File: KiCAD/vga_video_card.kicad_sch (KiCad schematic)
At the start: 4 parts, among them SW1 rst_btn, U5 74HC04, Y1 10MHz

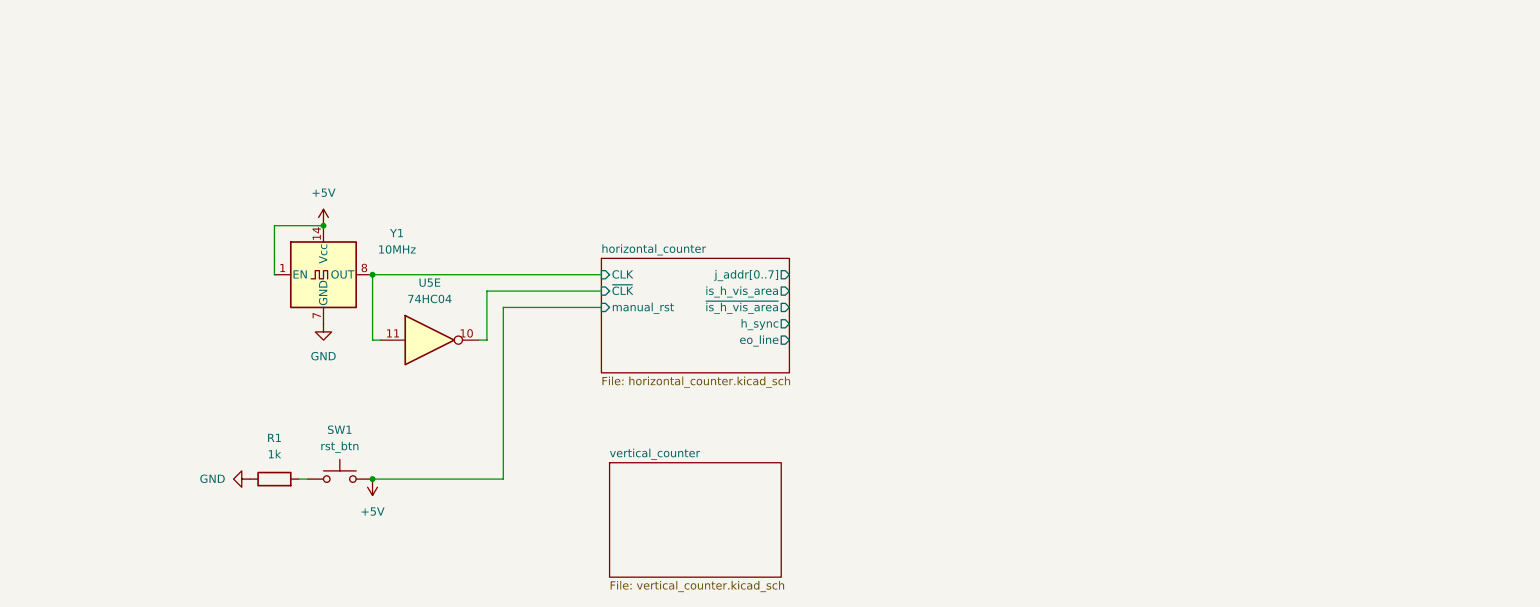
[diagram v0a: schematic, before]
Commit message: assigned footprints
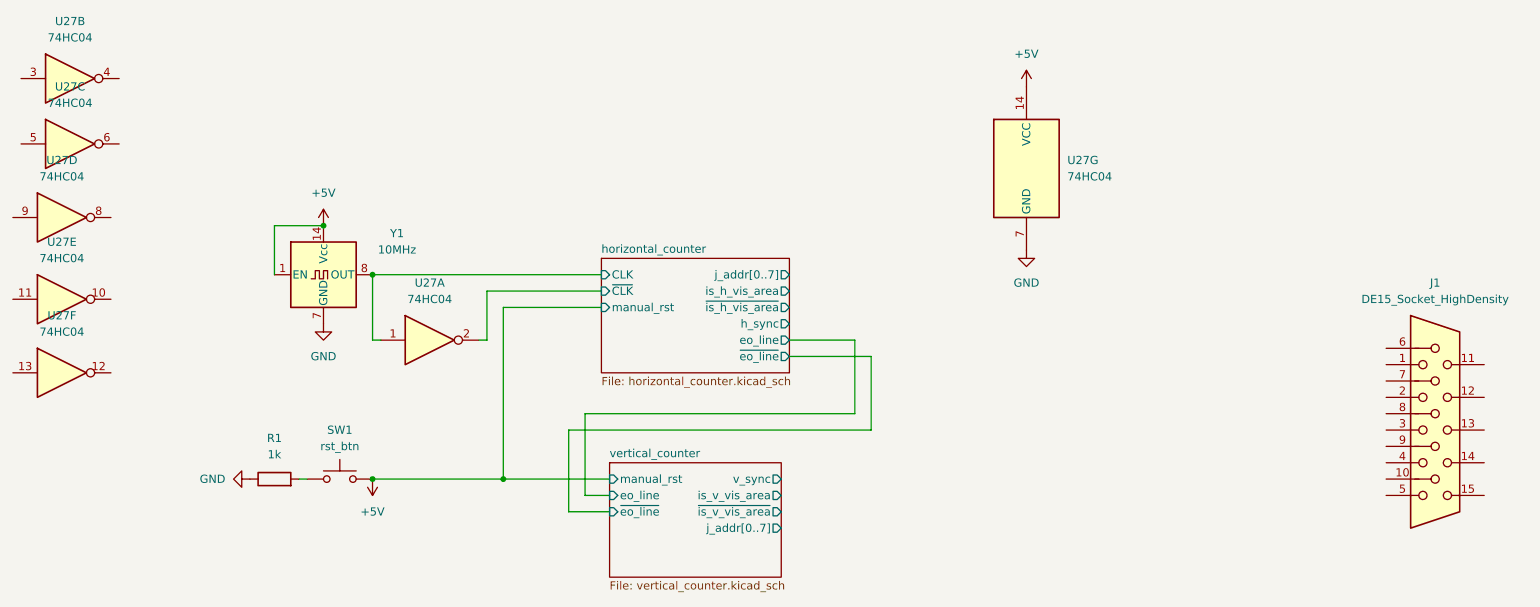
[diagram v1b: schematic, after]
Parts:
- removed U5: 74HC04, symbol 74xx:74HC04
- added J1: DE15_Socket_HighDensity, Connector_Dsub:DSUB-15_Socket_EdgeMount_P2.77mm, symbol Connector:DE15_Socket_HighDensity
- added U27: 74HC04, Package_DIP:DIP-14_W7.62mm, symbol 74xx:74HC04
- R1: footprint (none) -> Resistor_THT:R_Axial_DIN0207_L6.3mm_D2.5mm_P7.62mm_Horizontal
- SW1: footprint (none) -> Button_Switch_THT:SW_PUSH_6mm
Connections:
- net +5V: now also U27.14 (VCC)
- net GND: now also U27.7 (GND)
- net horizontal_counter/CLK: now also U27.1
- net horizontal_counter/~{CLK}: now also U27.2
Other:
- sheet horizontal_counter ports: added ~{eo_line}; removed none
- sheet vertical_counter ports: added eo_line, is_v_vis_area, j_addr[0..7], manual_rst, v_sync, ~{eo_line}, ~{is_v_vis_area}; removed none

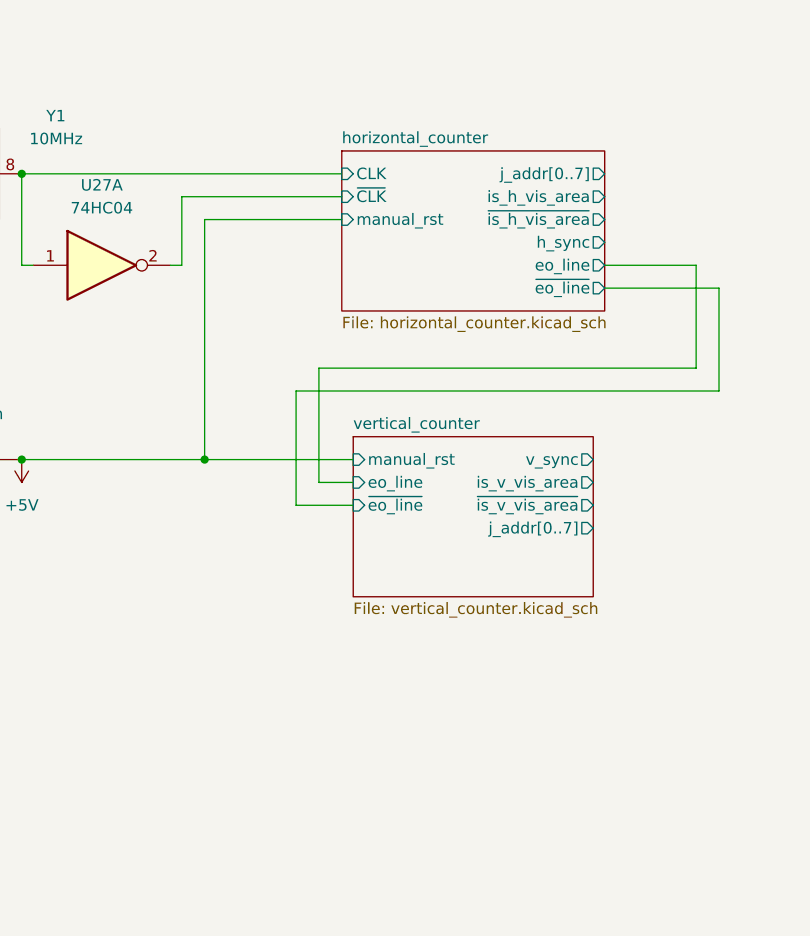
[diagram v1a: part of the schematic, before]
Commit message: finished most of the schematics of submodules except DAC, need to work on integration
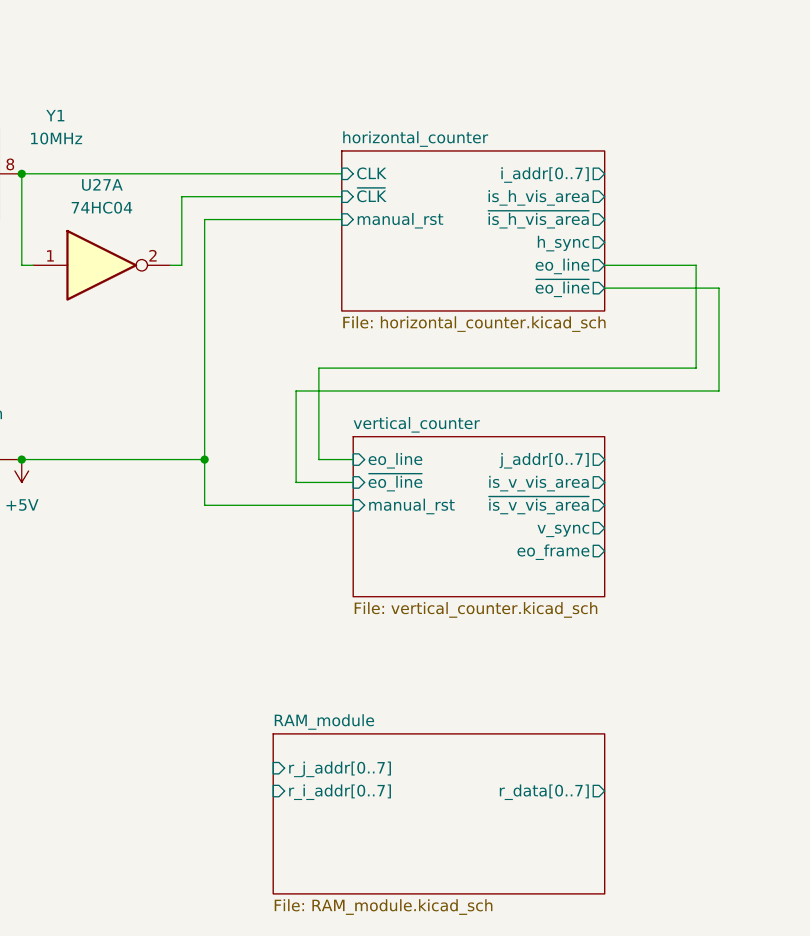
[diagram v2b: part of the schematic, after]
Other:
- added sheet RAM_module (RAM_module.kicad_sch)
- sheet horizontal_counter ports: added i_addr[0..7]; removed j_addr[0..7]
- sheet vertical_counter ports: added eo_frame; removed none
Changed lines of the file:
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@@
 	(wire
 		(pts
-			(xy 104.14 88.9) (xy 107.95 88.9)
+			(xy 91.44 91.44) (xy 91.44 86.36)
+		)
+		(stroke
+			(width 0)
+			(type default)
+		)
+	)
+	(wire
+		(pts
+			(xy 104.14 86.36) (xy 107.95 86.36)
 		)
 		(stroke
@@
 	(wire
 		(pts
-			(xy 91.44 86.36) (xy 107.95 86.36)
+			(xy 91.44 91.44) (xy 107.95 91.44)
 		)
 		(stroke
@@
 	(wire
 		(pts
-			(xy 101.6 91.44) (xy 101.6 78.74)
+			(xy 101.6 88.9) (xy 101.6 78.74)
 		)
 		(stroke
@@
 	(wire
 		(pts
-			(xy 107.95 91.44) (xy 101.6 91.44)
+			(xy 107.95 88.9) (xy 101.6 88.9)
 		)
 		(stroke
@@
 	(wire
 		(pts
-			(xy 104.14 76.2) (xy 104.14 88.9)
+			(xy 104.14 76.2) (xy 104.14 86.36)
 		)
 		(stroke
@@
 	(sheet
 		(at 107.95 83.82)
-		(size 26.67 17.78)
+		(size 27.94 17.78)
 		(exclude_from_sim no)
 		(in_bom yes)
@@
 		)
 		(pin "manual_rst" input
+			(at 107.95 91.44 180)
+			(effects
+				(font
+					(size 1.27 1.27)
+				)
+				(justify left)
+			)
+		)
+		(pin "eo_line" input
 			(at 107.95 86.36 180)
 			(effects
@@
 			)
 		)
-		(pin "eo_line" input
+		(pin "v_sync" output
+			(at 135.89 93.98 0)
+			(effects
+				(font
+					(size 1.27 1.27)
+				)
+				(justify right)
+			)
+		)
+		(pin "is_v_vis_area" output
+			(at 135.89 88.9 0)
+			(effects
+				(font
+					(size 1.27 1.27)
+				)
+				(justify right)
+			)
+		)
+		(pin "~{eo_line}" input
 			(at 107.95 88.9 180)
 			(effects
@@
 			)
 		)
-		(pin "v_sync" output
-			(at 134.62 86.36 0)
+		(pin "~{is_v_vis_area}" output
+			(at 135.89 91.44 0)
 			(effects
 				(font
@@
 			)
 		)
-		(pin "is_v_vis_area" output
-			(at 134.62 88.9 0)
+		(pin "j_addr[0..7]" output
+			(at 135.89 86.36 0)
 			(effects
 				(font
@@
 			)
 		)
-		(pin "~{eo_line}" input
-			(at 107.95 91.44 180)
-			(effects
-				(font
-					(size 1.27 1.27)
-				)
-				(justify left)
-			)
-		)
-		(pin "~{is_v_vis_area}" output
-			(at 134.62 91.44 0)
-			(effects
-				(font
-					(size 1.27 1.27)
-				)
-				(justify right)
-			)
-		)
-		(pin "j_addr[0..7]" output
-			(at 134.62 93.98 0)
+		(pin "eo_frame" output
+			(at 135.89 96.52 0)
 			(effects
 				(font
@@
 			)
 		)
-		(pin "j_addr[0..7]" output
-			(at 135.89 54.61 0)
-			(effects
-				(font
-					(size 1.27 1.27)
-				)
-				(justify right)
-			)
-		)
 		(pin "is_h_vis_area" output
 			(at 135.89 57.15 0)
@@
 			)
 		)
+		(pin "i_addr[0..7]" output
+			(at 135.89 54.61 0)
+			(effects
+				(font
+					(size 1.27 1.27)
+				)
+				(justify right)
+			)
+		)
 		(instances
 			(project "vga_video_card"
@@
 				)
 			)
+		)
+	)
+	(sheet
+		(at 99.06 116.84)
+		(size 36.83 17.78)
+		(exclude_from_sim no)
+		(in_bom yes)
+		(on_board yes)
+		(dnp no)
+		(fields_autoplaced yes)
+		(stroke
+			(width 0.1524)
+			(type solid)
+		)
+		(fill
+			(color 0 0 0 0.0000)
+		)
+		(property "Sheetname" "RAM_module"
+			(at 99.06 116.1284 0)
+			(effects
+				(font
+					(size 1.27 1.27)
+				)
+				(justify left bottom)
+			)
+		)
+		(property "Sheetfile" "RAM_module.kicad_sch"
+			(at 99.06 135.2046 0)
+			(effects
+				(font
+					(size 1.27 1.27)
+				)
+				(justify left top)
+			)
+		)
+		(pin "r_i_addr[0..7]" input
+			(at 99.06 123.19 180)
+			(effects
+				(font
+					(size 1.27 1.27)
+				)
+				(justify left)
+			)
+		)
+		(pin "r_data[0..7]" output
+			(at 135.89 123.19 0)
+			(effects
+				(font
+					(size 1.27 1.27)
+				)
+				(justify right)
+			)
+		)
+		(pin "r_j_addr[0..7]" input
+			(at 99.06 120.65 180)
+			(effects
+				(font
+					(size 1.27 1.27)
+				)
+				(justify left)
+			)
+		)
+		(instances
+			(project "vga_video_card"
+				(path "/53ebbfbe-eaa1-4706-acc1-611a99db7179"
+					(page "12")
+				)
+			)

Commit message: finished schematics and footprint assignments; need to figure out +5v connection issue
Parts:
- added J6: Conn_02x16_Counter_Clockwise, Connector_PinSocket_2.54mm:PinSocket_2x16_P2.54mm_Vertical, symbol Connector_Generic:Conn_02x16_Counter_Clockwise
- added R16, R17, R18: 1K, Resistor_THT:R_Axial_DIN0207_L6.3mm_D2.5mm_P7.62mm_Horizontal, symbol Device:R
- added RV2, RV3, RV4: 10K Pot, Potentiometer_THT:Potentiometer_Vishay_T73YP_Vertical, symbol Device:R_Potentiometer_Trim
- added SW2, SW3, SW4: SW_DPDT_x2, Button_Switch_THT:SW_CK_JS202011CQN_DPDT_Straight, symbol Switch:SW_DPDT_x2
- added U39: 74HC02, Package_DIP:DIP-14_W7.62mm, symbol 74xx:74HC02
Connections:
- net +5V: now also J6.1 (Pin_1), U39.14 (VCC)
- net GND: now also J1.10, J1.5, J1.6, J1.7, J1.8, J6.32 (Pin_32), R16.2, R17.2, R18.2, U39.7 (GND)
- net horizontal_counter/~{is_h_vis_area}: now also U39.2
- net vertical_counter/~{is_v_vis_area}: now also U39.3
- net VGA_R: now reaches J1.1
- net VGA_R: now also J6.12 (Pin_12), R16.1, RV2.1
- net h_sync: now reaches J1.13
- net h_sync: now also J6.15 (Pin_15)
- net v_sync: now reaches J1.14
- net v_sync: now also J6.16 (Pin_16)
- net VGA_G: now reaches J1.2
- net VGA_G: now also J6.13 (Pin_13), R17.1, RV3.1
- net VGA_B: now reaches J1.3
- net VGA_B: now also J6.14 (Pin_14), R18.1, RV4.1
- net horizontal_counter/manual_rst: now reaches R1.2, SW1.1
- new net: RV2.2, SW2.2 (B), SW2.5 (B)
- new net: RV4.2, SW4.2 (B), SW4.5 (B)
- new net: RV3.2, SW3.2 (B), SW3.5 (B)
- new net eo_frame: J6.11 (Pin_11)
- new net eo_line: J6.10 (Pin_10)
- new net ext_B: J6.18 (Pin_18), SW4.1 (A), SW4.4 (A)
- new net ext_G: J6.19 (Pin_19), SW3.1 (A), SW3.4 (A)
- new net ext_R: J6.20 (Pin_20), SW2.1 (A), SW2.4 (A)
- new net i_addr0: J6.2 (Pin_2)
- new net i_addr1: J6.3 (Pin_3)
- new net i_addr2: J6.4 (Pin_4)
- new net i_addr3: J6.5 (Pin_5)
- new net i_addr4: J6.6 (Pin_6)
- new net i_addr5: J6.7 (Pin_7)
- new net i_addr6: J6.8 (Pin_8)
- new net i_addr7: J6.9 (Pin_9)
- new net int_brightness: J6.17 (Pin_17), SW2.3 (C), SW2.6 (C), SW3.3 (C), SW3.6 (C), SW4.3 (C), SW4.6 (C)
- new net is_h_vis_area: J6.23 (Pin_23)
- new net is_v_vis_area: J6.22 (Pin_22)
- new net is_vis_area: J6.21 (Pin_21), U39.1
- new net j_addr_0: J6.31 (Pin_31)
- new net j_addr_1: J6.30 (Pin_30)
- new net j_addr_2: J6.29 (Pin_29)
- new net j_addr_3: J6.28 (Pin_28)
- new net j_addr_4: J6.27 (Pin_27)
- new net j_addr_5: J6.26 (Pin_26)
- new net j_addr_6: J6.25 (Pin_25)
- new net j_addr_7: J6.24 (Pin_24)
- no-connect marks 0 -> 19
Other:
- added sheet ADC_module (ADC_module.kicad_sch)
- sheet horizontal_counter ports: added j_addr[0..7]; removed i_addr[0..7]
- sheet vertical_counter ports: added i_addr[0..7]; removed j_addr[0..7]
- moved on the sheet: J1, R1, SW1, U27A, U27G, Y1

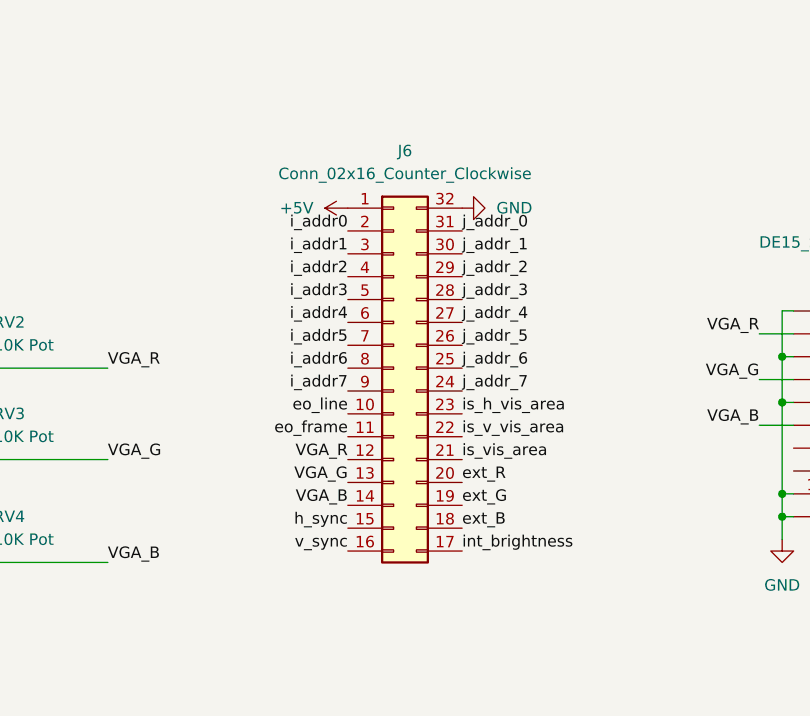
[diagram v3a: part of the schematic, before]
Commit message: fix footprint
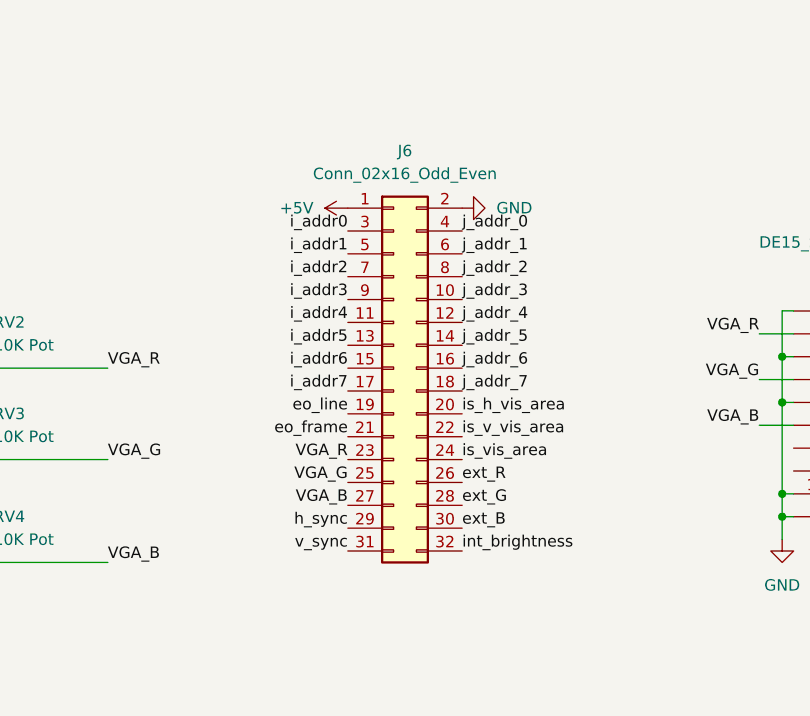
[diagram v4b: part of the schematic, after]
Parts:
- removed J6: Conn_02x16_Counter_Clockwise, Connector_PinSocket_2.54mm:PinSocket_2x16_P2.54mm_Vertical, symbol Connector_Generic:Conn_02x16_Counter_Clockwise
- added J6: Conn_02x16_Odd_Even, Connector_PinSocket_2.54mm:PinSocket_2x16_P2.54mm_Vertical, symbol Connector_Generic:Conn_02x16_Odd_Even
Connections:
- net +5V: now also J6.1 (Pin_1)
- net GND: now also J6.2 (Pin_2)
- net VGA_B: now also J6.27 (Pin_27)
- net VGA_G: now also J6.25 (Pin_25)
- net VGA_R: now also J6.23 (Pin_23)
- net eo_frame: now also J6.21 (Pin_21)
- net eo_line: now also J6.19 (Pin_19)
- net ext_B: now also J6.30 (Pin_30)
- net ext_G: now also J6.28 (Pin_28)
- net ext_R: now also J6.26 (Pin_26)
- net h_sync: now also J6.29 (Pin_29)
- net i_addr0: now also J6.3 (Pin_3)
- net i_addr1: now also J6.5 (Pin_5)
- net i_addr2: now also J6.7 (Pin_7)
- net i_addr3: now also J6.9 (Pin_9)
- net i_addr4: now also J6.11 (Pin_11)
- net i_addr5: now also J6.13 (Pin_13)
- net i_addr6: now also J6.15 (Pin_15)
- net i_addr7: now also J6.17 (Pin_17)
- net int_brightness: now also J6.32 (Pin_32)
- net is_h_vis_area: now also J6.20 (Pin_20)
- net is_v_vis_area: now also J6.22 (Pin_22)
- net is_vis_area: now also J6.24 (Pin_24)
- net j_addr_0: now also J6.4 (Pin_4)
- net j_addr_1: now also J6.6 (Pin_6)
- net j_addr_2: now also J6.8 (Pin_8)
- net j_addr_3: now also J6.10 (Pin_10)
- net j_addr_4: now also J6.12 (Pin_12)
- net j_addr_5: now also J6.14 (Pin_14)
- net j_addr_6: now also J6.16 (Pin_16)
- net j_addr_7: now also J6.18 (Pin_18)
- net v_sync: now also J6.31 (Pin_31)
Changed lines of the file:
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@@
+	)
+	(symbol
+		(lib_id "Connector_Generic:Conn_02x16_Odd_Even")
+		(at 180.34 135.89 0)
+		(unit 1)
+		(exclude_from_sim no)
+		(in_bom yes)
+		(on_board yes)
+		(dnp no)
+		(fields_autoplaced yes)
+		(property "Reference" "J6"
+			(at 181.61 111.76 0)
+			(effects
+				(font
+					(size 1.27 1.27)
+				)
+			)
+		)
+		(property "Value" "Conn_02x16_Odd_Even"
+			(at 181.61 114.3 0)
+			(effects
+				(font
+					(size 1.27 1.27)
+				)
+			)
+		)
+		(property "Footprint" "Connector_PinSocket_2.54mm:PinSocket_2x16_P2.54mm_Vertical"
+			(at 180.34 135.89 0)
+			(effects
+				(font
+					(size 1.27 1.27)
+				)
+				(hide yes)
+			)
+		)
+		(property "Datasheet" "~"
+			(at 180.34 135.89 0)
+			(effects
+				(font
+					(size 1.27 1.27)
+				)
+				(hide yes)
+			)
+		)
+		(property "Description" "Generic connector, double row, 02x16, odd/even pin numbering scheme (row 1 odd numbers, row 2 even numbers), script generated (kicad-library-utils/schlib/autogen/connector/)"
+			(at 180.34 135.89 0)
+			(effects
+				(font
+					(size 1.27 1.27)
+				)
+				(hide yes)
+			)
+		)
+		(pin "17"
+		)
+		(pin "29"
+		)
+		(pin "2"
+		)
+		(pin "21"
+		)
+		(pin "3"
+		)
+		(pin "1"
+		)
+		(pin "7"
+		)
+		(pin "23"
+		)
+		(pin "25"
+		)
+		(pin "9"
+		)
+		(pin "11"
+		)
+		(pin "13"
+		)
+		(pin "15"
+		)
+		(pin "5"
+		)
+		(pin "19"
+		)
+		(pin "27"
+		)
+		(pin "31"
+		)
+		(pin "10"
+		)
+		(pin "4"
+		)
+		(pin "28"
+		)
+		(pin "30"
+		)
+		(pin "32"
+		)
+		(pin "18"
+		)
+		(pin "16"
+		)
+		(pin "6"
+		)
+		(pin "20"
+		)
+		(pin "8"
+		)
+		(pin "22"
+		)
+		(pin "12"
+		)
+		(pin "26"
+		)
+		(pin "14"
+		)
+		(pin "24"
+		)
+		(instances
+			(project ""
+				(path "/53ebbfbe-eaa1-4706-acc1-611a99db7179"
+					(reference "J6")
+					(unit 1)
+				)
+			)
+		)
 	)
 	(symbol
@@
 					(unit 1)
 				)
-			)
-		)
-	)
-	(symbol
-		(lib_id "Connector_Generic:Conn_02x16_Counter_Clockwise")
-		(at 180.34 135.89 0)
-		(unit 1)
-		(exclude_from_sim no)
-		(in_bom yes)
-		(on_board yes)
-		(dnp no)
-		(fields_autoplaced yes)
-		(property "Reference" "J6"
-			(at 181.61 111.76 0)
-			(effects
-				(font
-					(size 1.27 1.27)
-				)
-			)
-		)
-		(property "Value" "Conn_02x16_Counter_Clockwise"
-			(at 181.61 114.3 0)
-			(effects
-				(font
-					(size 1.27 1.27)
-				)
-			)
-		)
-		(property "Footprint" "Connector_PinSocket_2.54mm:PinSocket_2x16_P2.54mm_Vertical"
-			(at 180.34 135.89 0)
-			(effects
-				(font
-					(size 1.27 1.27)
-				)
-				(hide yes)
-			)
-		)
-		(property "Datasheet" "~"
-			(at 180.34 135.89 0)
-			(effects
-				(font
-					(size 1.27 1.27)
-				)
-				(hide yes)
-			)
-		)
-		(property "Description" "Generic connector, double row, 02x16, counter clockwise pin numbering scheme (similar to DIP package numbering), script generated (kicad-library-utils/schlib/autogen/connector/)"
-			(at 180.34 135.89 0)
-			(effects
-				(font
-					(size 1.27 1.27)
-				)
-				(hide yes)
-			)
-		)
-		(pin "20"
-		)
-		(pin "21"
-		)
-		(pin "19"
-		)
-		(pin "18"
-		)
-		(pin "17"
-		)
-		(pin "7"
-		)
-		(pin "8"
-		)
-		(pin "9"
-		)
-		(pin "11"
-		)
-		(pin "10"
-		)
-		(pin "13"
-		)
-		(pin "14"
-		)
-		(pin "15"
-		)
-		(pin "12"
-		)
-		(pin "28"
-		)
-		(pin "31"
-		)
-		(pin "30"
-		)
-		(pin "23"
-		)
-		(pin "24"
-		)
-		(pin "16"
-		)
-		(pin "29"
-		)
-		(pin "32"
-		)
-		(pin "26"
-		)
-		(pin "25"
-		)
-		(pin "27"
-		)
-		(pin "22"
-		)
-		(pin "1"
-		)
-		(pin "2"
-		)
-		(pin "3"
-		)
-		(pin "4"
-		)
-		(pin "6"
-		)
-		(pin "5"
-		)
-		(instances
-			(project ""
-				(path "/53ebbfbe-eaa1-4706-acc1-611a99db7179"
-					(reference "J6")
-					(unit 1)
-				)
